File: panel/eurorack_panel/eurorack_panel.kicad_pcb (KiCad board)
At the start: 2 copper layers, 101.6 x 128.6 mm, 2 parts

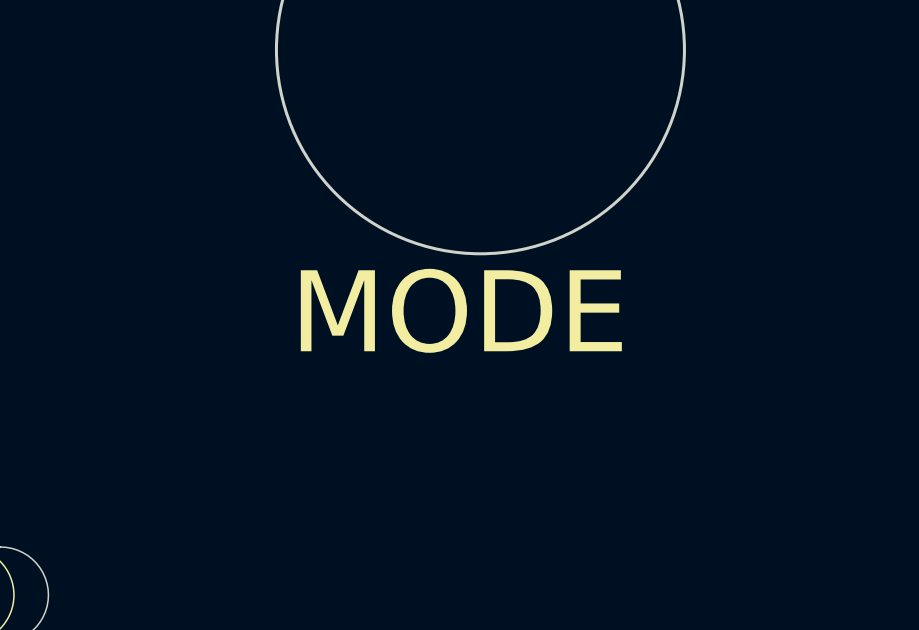
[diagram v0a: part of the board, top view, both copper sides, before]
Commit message: update hardware to v1_1_0 plus small panel updates
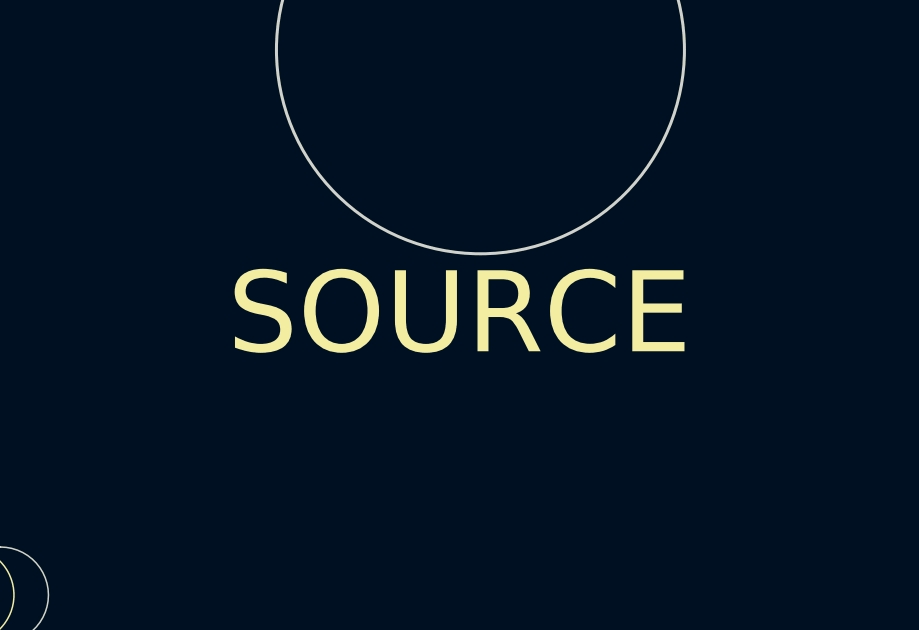
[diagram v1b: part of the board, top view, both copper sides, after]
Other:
- board text added: "SOURCE"
- board text added: "cyberboy666 & ichi raramuri recurBOY panel for v1_0_0 mk_i"
- board text removed: "MODE"
- board text removed: "cyberboy666 & ichi raramuri recurBOY panel for v0_7_1 mk_iii"
